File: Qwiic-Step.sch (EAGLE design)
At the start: 56 parts, among them J1 PTH, J2 Qwiic Right Angle, J3 POWER_JACKSUPER_BOMB_DIGITY, J4 Qwiic Right Angle, J7 ISP, U1 A49885MM, U4 ATTINY84-ARDUINO

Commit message: temporary 4 layer
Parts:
- removed FID1, FID2: FIDUCIAL1X2, SparkFun-Aesthetics:FIDUCIAL1X2
- removed J8: (no value), SparkFun-Connectors:CONN_01PTH_NO_SILK_YES_STOP
- removed JP3: JUMPER-SMT_2_NC_TRACE_SILK, SparkFun-Jumpers:JUMPER-SMT_2_NC_TRACE_SILK
- removed JP4: JUMPER-SMT_3_2-NC_TRACE_SILK, SparkFun-Jumpers:JUMPER-SMT_3_2-NC_TRACE_SILK
- removed JP5: (no value), BigEasyDriver_v11:M04SCREW_LOCK
- removed LED2: Yellow, SparkFun-LED:LED-YELLOWLILYPAD
- removed LOGO2: SFE_LOGO_NAME_FLAME.1_INCH, SparkFun-Aesthetics:SFE_LOGO_NAME_FLAME.1_INCH
- removed R13: 8.2k, SparkFun-Resistors:8.2KOHM-0603-1/10W-5%
- removed R16: 10k, SparkFun-Resistors:TRIMPOT-SMD-3MM-CLOSED-1/8W-20%
- removed R6, R7: 2.2k, SparkFun-Resistors:2.2KOHM-0603-1/10W-1%
- removed R8: 10k, SparkFun-Resistors:10KOHM-0603-1/10W-1%
- removed R9: 1k, SparkFun-Resistors:1KOHM-0603-1/10W-1%
- removed TP2: TEST-POINT3X4, SparkFun-Connectors:TEST-POINT3X4
- removed U4: ATTINY84-ARDUINO, SparkFun-IC-Microcontroller:ATTINY84-ARDUINO
- added C14, C5: 0.1uF, SparkFun-Capacitors:0.1UF-0603-25V-(+80/-20%)
- added D4: RED, SparkFun-LED:LED-RED0603
- added D5: Yellow, SparkFun-LED:LED-YELLOW0603
- added J5: ISP, SparkFun-Connectors:AVR_SPI_PROG_3X2PTH
- added J9: (no value), SparkFun-Connectors:CONN_023.5MM
- added JP13: JUMPER-SMT_2_NC_TRACE_SILK, SparkFun-Jumpers:JUMPER-SMT_2_NC_TRACE_SILK
- added R12: 4.7k, SparkFun-Resistors:4.7KOHM-0603-1/10W-1%
- added R14: 10k, SparkFun-Resistors:10KOHM-0603-1/10W-1%
- added R15: 1k, SparkFun-Resistors:1KOHM-0603-1/10W-1%
- added S1: Tall Switch, SparkFun-Switches:MOMENTARY-SWITCH-SPST-SMD-5.2-TALL-REDUNDANT
- added U2: ATMEGA328P_TQFP, SparkFun-IC-Microcontroller:ATMEGA328P_TQFP
- added Y1: 16MHz, SparkFun-Clocks:RESONATOR-16MHZSMD_3.2X1.3
- C2: value 0.1uF -> 10nF; device SparkFun-Capacitors:0.1UF-0603-25V-(+80/-20%) -> SparkFun-Capacitors:10NF-0603-50V-10%
- C4: value 10uF -> 0.1uF; device SparkFun-Capacitors:10UF-0603-6.3V-20% -> SparkFun-Capacitors:0.1UF-0603-100V-10%
- D2: value RED -> GREEN; device SparkFun-LED:LED-RED0603 -> SparkFun-LED:LED-GREEN0603
- J6: device SparkFun-Connectors:CONN_01PTH_NO_SILK_YES_STOP -> SparkFun-Connectors:CONN_04SCREW
- J7: value ISP -> (none); device SparkFun-Connectors:AVR_SPI_PROG_3X2TESTPOINTS -> SparkFun-Connectors:CONN_06NO_SILK_NO_POP
- JP2: value JUMPER-SMT_2_NO_SILK -> INT; device SparkFun-Jumpers:JUMPER-SMT_2_NO_SILK -> SparkFun-Jumpers:JUMPER-SMT_2_NC_TRACE_SILK
- R3: value 100k -> 33k; device SparkFun-Resistors:100KOHM-0603-1/10W-1% -> SparkFun-Resistors:33KOHM-0603-1/10W-1%
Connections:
- removed net !INT!: R2.1, U4.(A0)0
- removed net !RST: J7.5, R8.1, U4.(!RESET!)11
- removed net N$2: D2.A, R9.1
- removed net N$3: R13.2, R16.CCW
- removed net N$5 (its old number): JP3.1, R9.2
- removed net SCL_PU1: JP4.1, R6.2
- removed net SDA_PU1: JP4.3, R7.2
- new net !RST!: C4.2, J5.5, R14.1, S1.2, U2.PC6(/RESET)
- new net AREF: C5.1, U2.AREF
- new net DTR: C4.1, J7.1
- new net INT: R2.1, U2.PD2(INT0)
- new net N$12: D2.A, R12.2
- new net N$13: U2.PB6(XTAL1/TOSC1), Y1.1
- new net N$14: U2.PB7(XTAL2/TOSC2), Y1.3
- new net N$26: D4.A, R15.1
- new net N$27: JP13.1, R15.2
- new net RXI: J7.3, U2.PD0(RXD)
- new net SCK: R12.1, U2.PB5(SCK)
- new net TXO: J7.2, U2.PD1(TXD)
- net !ENABLE!: now also U2.PB3(MOSI/OC2); no longer U4.(A2)2
- net !RESET!: now also U2.PB0(ICP)
- net !SLEEP!: now also U2.PD4(XCK/T0)
- net 3.3V: now also C14.1, J5.2, JP13.2, R14.2, U2.AVCC, U2.VCC; no longer C2.1, J7.2, JP3.2, JP4.2, R13.1, R8.2, U4.VCC
- net ADR: now also U2.PB1(OC1A); no longer U4.(A1)1
- net COILA+: now also J6.1; no longer JP5.4
- net COILA-: now also J6.2; no longer JP5.3
- net COILB+: now also J6.4; no longer JP5.1
- net COILB-: now also J6.3; no longer JP5.2
- net CUR_REF: now also C2.1; no longer C4.2, R16.WIPER, TP2.1
- net CUR_REF_PWM: now also U2.PD3(INT1); no longer U4.(INT0)~8
- net DIR: now also U2.PB2(SS/OC1B); no longer U4.(A3)3
- net GND: now also C14.2, C5.2, D4.C, D5.C, J5.6, J7.5, J9.1, S1.1, U2.AGND, U2.GND, Y1.2; no longer C4.1, J8.1, LED2.C, R16.CW, U4.GND
- net MS1: now also J5.1, U2.PD7(AIN1); no longer J7.1, U4.(TX/MISO/A5)~5
- net MS2: now also U2.PD6(AIN0); no longer U4.(XTAL2)9
- net MS3: now also U2.PD5(T1); no longer U4.(XTAL1)10
- net N$10: now also D5.A; no longer LED2.A
- net N$7: now also J9.2; no longer J6.1
- net SCL: now also J5.3, U2.PC5(ADC5/SCL); no longer J7.3, R6.1, U4.(SCL/SCK/A4)4
- net SDA: now also J5.4, U2.PC4(ADC4/SDA); no longer J7.4, R7.1, U4.(RX/SDA/MOSI/A6)~6
- net STEP: now also U2.ADC7; no longer U4.(A7)~7
- net VIN: now also J7.4
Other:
- note added: "ATmega328"
- note added: "RXI"
- note added: "TXO"
- note removed: "7-Bit Unshifted I2C Address Open Jumper (Default): 0x52 Closed Jumper: 0x51 Software configurable as well"
- note removed: "ATtiny Controller"
- note removed: "I2C Pull Ups"
- moved on the sheet: C10, C2, C4, D2, D3, J1, J2, J4, JP11, JP6, R10, R11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

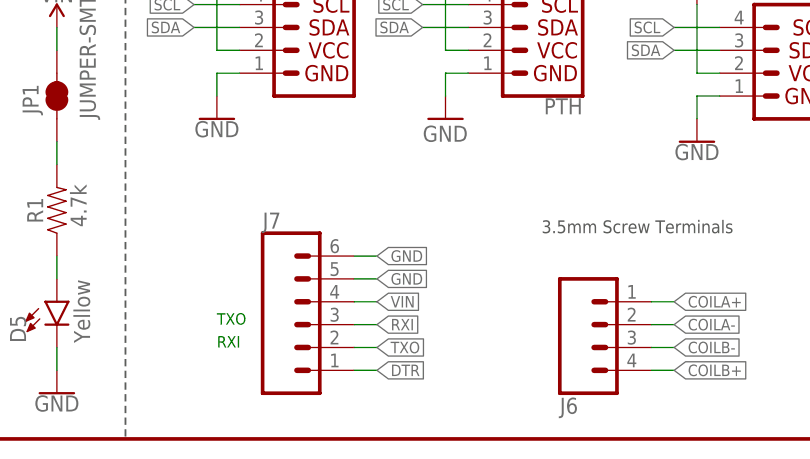
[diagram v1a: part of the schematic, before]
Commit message: Reduce to 2 layers
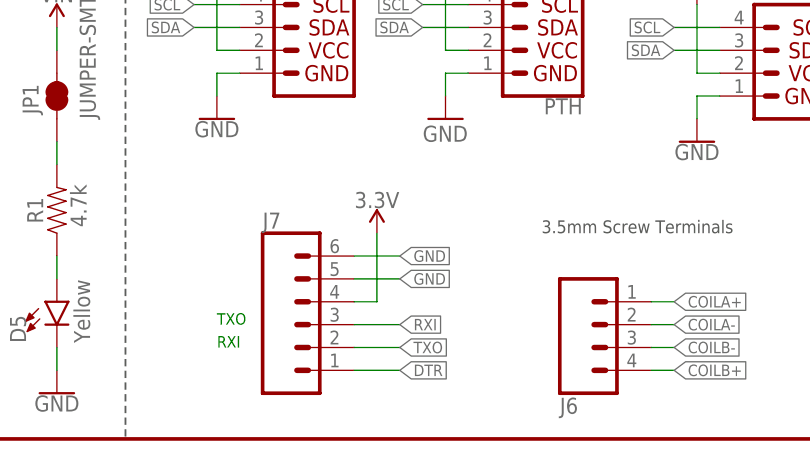
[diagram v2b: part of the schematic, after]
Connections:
- net 3.3V: now also J7.4
- net VIN: no longer J7.4
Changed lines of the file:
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@@
 <?xml version="1.0" encoding="utf-8"?>
 <!DOCTYPE eagle SYSTEM "eagle.dtd">
-<eagle version="9.4.2">
+<eagle version="9.5.1">
 <drawing>
 <settings>
@@
 <part name="C4" library="SparkFun-Capacitors" deviceset="0.1UF" device="-0603-100V-10%" value="0.1uF"/>
 <part name="J6" library="SparkFun-Connectors" deviceset="CONN_04" device="SCREW"/>
+<part name="SUPPLY5" library="SparkFun-PowerSymbols" deviceset="3.3V" device=""/>
 </parts>
 <sheets>
@@
 <attribute name="NAME" x="111.76" y="4.572" size="1.778" layer="95" font="vector" rot="MR180"/>
 </instance>
+<instance part="SUPPLY5" gate="G$1" x="91.44" y="22.86" smashed="yes">
+<attribute name="VALUE" x="91.44" y="25.654" size="1.778" layer="96" align="bottom-center"/>
+</instance>
 </instances>
 <busses>
@@
 <segment>
 <pinref part="J7" gate="G$1" pin="6"/>
-<wire x1="88.9" y1="20.32" x2="91.44" y2="20.32" width="0.1524" layer="91"/>
-<label x="91.44" y="20.32" size="1.27" layer="95" xref="yes"/>
+<wire x1="88.9" y1="20.32" x2="93.98" y2="20.32" width="0.1524" layer="91"/>
+<label x="93.98" y="20.32" size="1.27" layer="95" xref="yes"/>
 </segment>
 <segment>
 <pinref part="J7" gate="G$1" pin="5"/>
-<wire x1="88.9" y1="17.78" x2="91.44" y2="17.78" width="0.1524" layer="91"/>
-<label x="91.44" y="17.78" size="1.27" layer="95" xref="yes"/>
+<wire x1="88.9" y1="17.78" x2="93.98" y2="17.78" width="0.1524" layer="91"/>
+<label x="93.98" y="17.78" size="1.27" layer="95" xref="yes"/>
 </segment>
 </net>
@@
 <wire x1="233.68" y1="139.7" x2="233.68" y2="142.24" width="0.1524" layer="91"/>
 </segment>
+<segment>
+<pinref part="J7" gate="G$1" pin="4"/>
+<wire x1="88.9" y1="15.24" x2="91.44" y2="15.24" width="0.1524" layer="91"/>
+<wire x1="91.44" y1="15.24" x2="91.44" y2="22.86" width="0.1524" layer="91"/>
+<pinref part="SUPPLY5" gate="G$1" pin="3.3V"/>
+</segment>
 </net>
 <net name="SCL" class="0">
@@
 <pinref part="SUPPLY14" gate="G$1" pin="VIN"/>
 <wire x1="55.88" y1="45.72" x2="55.88" y2="43.18" width="0.1524" layer="91"/>
-</segment>
-<segment>
-<pinref part="J7" gate="G$1" pin="4"/>
-<wire x1="88.9" y1="15.24" x2="91.44" y2="15.24" width="0.1524" layer="91"/>
-<label x="91.44" y="15.24" size="1.27" layer="95" xref="yes"/>
 </segment>
 </net>
@@
 <segment>
 <pinref part="J7" gate="G$1" pin="1"/>
-<wire x1="88.9" y1="7.62" x2="91.44" y2="7.62" width="0.1524" layer="91"/>
-<label x="91.44" y="7.62" size="1.27" layer="95" xref="yes"/>
+<wire x1="88.9" y1="7.62" x2="93.98" y2="7.62" width="0.1524" layer="91"/>
+<label x="93.98" y="7.62" size="1.27" layer="95" xref="yes"/>
 </segment>
 <segment>
@@
 <segment>
 <pinref part="J7" gate="G$1" pin="3"/>
-<wire x1="88.9" y1="12.7" x2="91.44" y2="12.7" width="0.1524" layer="91"/>
-<label x="91.44" y="12.7" size="1.27" layer="95" xref="yes"/>
+<wire x1="88.9" y1="12.7" x2="93.98" y2="12.7" width="0.1524" layer="91"/>
+<label x="93.98" y="12.7" size="1.27" layer="95" xref="yes"/>
 </segment>
 </net>
@@
 <segment>
 <pinref part="J7" gate="G$1" pin="2"/>
-<wire x1="88.9" y1="10.16" x2="91.44" y2="10.16" width="0.1524" layer="91"/>
-<label x="91.44" y="10.16" size="1.27" layer="95" xref="yes"/>
-</segment>
-</net>
+<wire x1="88.9" y1="10.16" x2="93.98" y2="10.16" width="0.1524" layer="91"/>
+<label x="93.98" y="10.16" size="1.27" layer="95" xref="yes"/>
+</segment>
+</net>
